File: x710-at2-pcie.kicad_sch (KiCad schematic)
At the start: 10 parts, among them U1 EZX710AT2_S_LMR5

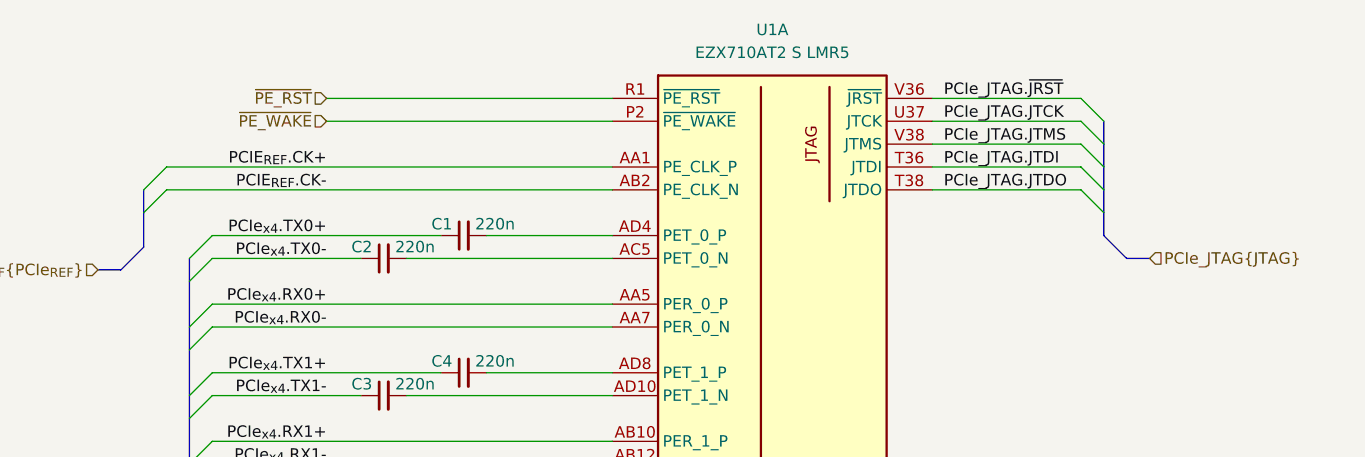
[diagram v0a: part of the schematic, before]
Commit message: [#80813] Add RJ45 connectors, add SMBus, FLASH SPI and misc
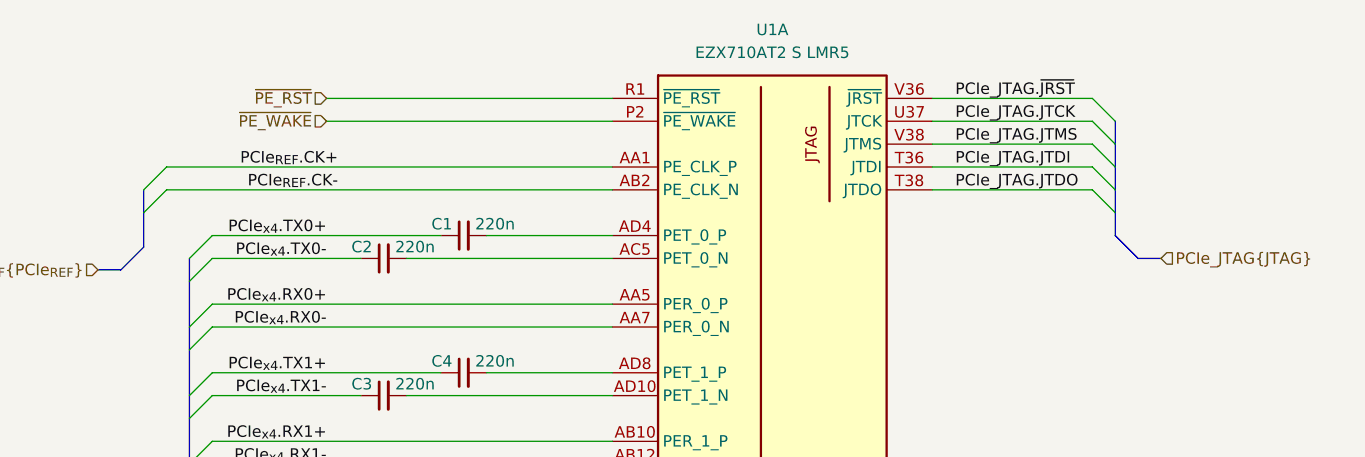
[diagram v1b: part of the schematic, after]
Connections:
- net PCIE_{REF}.CK+ renamed PCIe_{REF}.CK+
- net PCIE_{REF}.CK- renamed PCIe_{REF}.CK-
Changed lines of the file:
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@@
 		(comment 1 "www.antmicro.com")
+	)
+	(bus_alias "JTAG"
+		(members "~{JRST}" "JTCK" "JTMS" "JTDI" "JTDO")
+	)
+	(bus_alias "PCIe"
+		(members "TX7+" "TX7-" "TX6+" "TX6-" "TX5+" "TX5-" "TX4+" "TX4-" "TX3+"
+			"TX3-" "TX2+" "TX2-" "TX1+" "TX1-" "TX0+" "TX0-" "RX7+" "RX7-" "RX6+"
+			"RX6-" "RX5+" "RX5-" "RX4+" "RX4-" "RX3+" "RX3-" "RX2+" "RX2-" "RX1+"
+			"RX1-" "RX0+" "RX0-"
+		)
 	)
 	(bus_alias "PCIe_{REF}"
@@
 	)
 	(bus_entry
-		(at 248.92 102.87)
+		(at 250.19 102.87)
 		(size -2.54 -2.54)
 		(stroke
@@
 	)
 	(bus_entry
-		(at 248.92 100.33)
+		(at 250.19 100.33)
 		(size -2.54 -2.54)
 		(stroke
@@
 	)
 	(bus_entry
-		(at 248.92 95.25)
+		(at 250.19 95.25)
 		(size -2.54 -2.54)
 		(stroke
@@
 	)
 	(bus_entry
-		(at 248.92 97.79)
+		(at 250.19 97.79)
 		(size -2.54 -2.54)
 		(stroke
@@
 	)
 	(bus_entry
-		(at 248.92 105.41)
+		(at 250.19 105.41)
 		(size -2.54 -2.54)
 		(stroke
@@
 		)
 	)
-	(wire
-		(pts
-			(xy 229.87 92.71) (xy 246.38 92.71)
-		)
-		(stroke
-			(width 0)
-			(type default)
-		)
-	)
 	(bus
 		(pts
@@
 		)
 	)
-	(wire
-		(pts
-			(xy 229.87 95.25) (xy 246.38 95.25)
-		)
-		(stroke
-			(width 0)
-			(type default)
-		)
-	)
-	(bus
-		(pts
-			(xy 248.92 105.41) (xy 248.92 107.95)
+	(bus
+		(pts
+			(xy 250.19 105.41) (xy 250.19 107.95)
 		)
 		(stroke
@@
 	(wire
 		(pts
-			(xy 229.87 97.79) (xy 246.38 97.79)
-		)
-		(stroke
-			(width 0)
-			(type default)
-		)
-	)
-	(wire
-		(pts
 			(xy 149.86 133.35) (xy 194.31 133.35)
 		)
@@
 		)
 	)
-	(bus
-		(pts
-			(xy 251.46 110.49) (xy 254 110.49)
+	(wire
+		(pts
+			(xy 229.87 95.25) (xy 247.65 95.25)
+		)
+		(stroke
+			(width 0)
+			(type default)
+		)
+	)
+	(bus
+		(pts
+			(xy 252.73 110.49) (xy 255.27 110.49)
 		)
 		(stroke
@@
 		)
 	)
-	(bus
-		(pts
-			(xy 248.92 97.79) (xy 248.92 100.33)
+	(wire
+		(pts
+			(xy 229.87 92.71) (xy 247.65 92.71)
+		)
+		(stroke
+			(width 0)
+			(type default)
+		)
+	)
+	(bus
+		(pts
+			(xy 250.19 97.79) (xy 250.19 100.33)
 		)
 		(stroke
@@
 	(wire
 		(pts
+			(xy 229.87 100.33) (xy 247.65 100.33)
+		)
+		(stroke
+			(width 0)
+			(type default)
+		)
+	)
+	(wire
+		(pts
 			(xy 149.86 130.81) (xy 194.31 130.81)
 		)
@@
 	(wire
 		(pts
+			(xy 229.87 102.87) (xy 247.65 102.87)
+		)
+		(stroke
+			(width 0)
+			(type default)
+		)
+	)
+	(wire
+		(pts
 			(xy 180.34 123.19) (xy 194.31 123.19)
 		)
@@
 	(bus
 		(pts
-			(xy 251.46 110.49) (xy 248.92 107.95)
+			(xy 252.73 110.49) (xy 250.19 107.95)
 		)
 		(stroke
@@
 	(wire
 		(pts
-			(xy 229.87 102.87) (xy 246.38 102.87)
-		)
-		(stroke
-			(width 0)
-			(type default)
-		)
-	)
-	(wire
-		(pts
 			(xy 171.45 125.73) (xy 194.31 125.73)
 		)
@@
 	(bus
 		(pts
-			(xy 248.92 102.87) (xy 248.92 105.41)
+			(xy 250.19 102.87) (xy 250.19 105.41)
 		)
 		(stroke
@@
 	(wire
 		(pts
+			(xy 229.87 97.79) (xy 247.65 97.79)
+		)
+		(stroke
+			(width 0)
+			(type default)
+		)
+	)
+	(wire
+		(pts
 			(xy 149.86 115.57) (xy 194.31 115.57)
 		)
@@
 		)
 	)
-	(wire
-		(pts
-			(xy 229.87 100.33) (xy 246.38 100.33)
-		)
-		(stroke
-			(width 0)
-			(type default)
-		)
-	)
-	(bus
-		(pts
-			(xy 248.92 100.33) (xy 248.92 102.87)
-		)
-		(stroke
-			(width 0)
-			(type default)
-		)
-	)
-	(bus
-		(pts
-			(xy 248.92 95.25) (xy 248.92 97.79)
+	(bus
+		(pts
+			(xy 250.19 100.33) (xy 250.19 102.87)
+		)
+		(stroke
+			(width 0)
+			(type default)
+		)
+	)
+	(bus
+		(pts
+			(xy 250.19 95.25) (xy 250.19 97.79)
 		)
 		(stroke
@@
 	)
 	(label "PCIe_JTAG.~{JRST}"
-		(at 231.14 92.71 0)
+		(at 232.41 92.71 0)
 		(effects
 			(font
@@
 	)
 	(label "PCIe_JTAG.JTDI"
-		(at 231.14 100.33 0)
+		(at 232.41 100.33 0)
 		(effects
 			(font
@@
 	)
 	(label "PCIe_JTAG.JTMS"
-		(at 231.14 97.79 0)
+		(at 232.41 97.79 0)
 		(effects
 			(font
@@
 		)
 	)
+	(label "PCIe_{REF}.CK-"
+		(at 163.83 102.87 180)
+		(effects
+			(font
+				(size 1.27 1.27)
+			)
+			(justify right bottom)
+		)
+	)
 	(label "PCIe_{x4}.TX0+"
 		(at 162.56 107.95 180)
@@
 		)
 	)
-	(label "PCIE_{REF}.CK-"
-		(at 162.56 102.87 180)
-		(effects
-			(font
-				(size 1.27 1.27)
-			)
-			(justify right bottom)
-		)
-	)
-	(label "PCIE_{REF}.CK+"
-		(at 162.56 100.33 180)
-		(effects
-			(font
-				(size 1.27 1.27)
-			)
-			(justify right bottom)
-		)
-	)
 	(label "PCIe_{x4}.RX1+"
 		(at 162.56 130.81 180)
@@
 	)
 	(label "PCIe_JTAG.JTCK"
-		(at 231.14 95.25 0)
+		(at 232.41 95.25 0)
 		(effects
 			(font
@@
 			)
 			(justify left bottom)
+		)
+	)
+	(label "PCIe_{REF}.CK+"
+		(at 163.83 100.33 180)
+		(effects
+			(font
+				(size 1.27 1.27)
+			)
+			(justify right bottom)
 		)
 	)
@@
 	)
 	(label "PCIe_JTAG.JTDO"
-		(at 231.14 102.87 0)
+		(at 232.41 102.87 0)
 		(effects
 			(font
@@
 	(hierarchical_label "PCIe_JTAG{JTAG}"
 		(shape input)
-		(at 254 110.49 0)
-		(effects
-			(font
+		(at 255.27 110.49 0)
+		(effects
+			(font

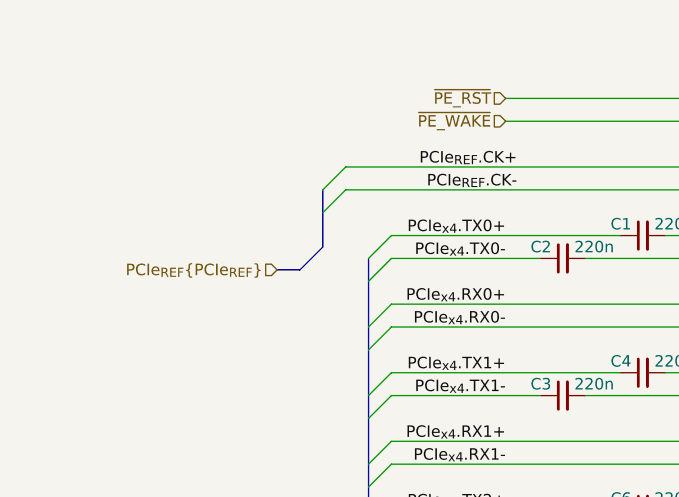
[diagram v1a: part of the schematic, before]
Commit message: [#80813] Add misc, improve schematic readability
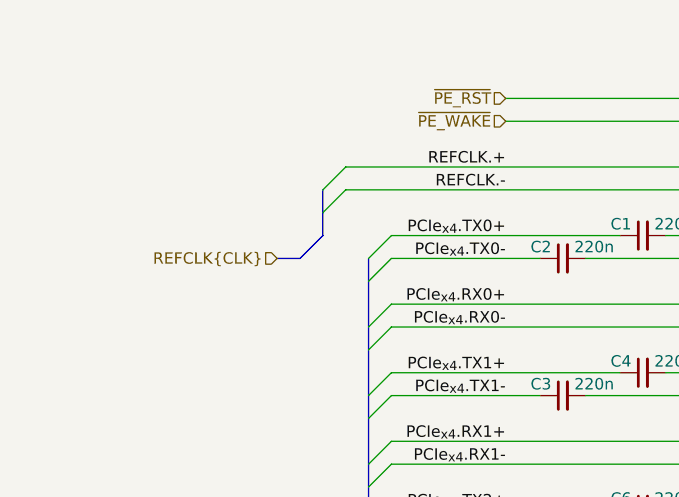
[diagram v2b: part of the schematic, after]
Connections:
- net PCIe_{REF}.CK+ renamed REFCLK.+
- net PCIe_{REF}.CK- renamed REFCLK.-
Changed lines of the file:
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@@
 		(comment 1 "www.antmicro.com")
+	)
+	(bus_alias "CLK"
+		(members "+" "-")
 	)
 	(bus_alias "JTAG"
@@
 		)
 	)
-	(bus_alias "PCIe_{REF}"
-		(members "CK+" "CK-")
-	)
 	(no_connect
 		(at 194.31 171.45)
@@
 	(bus
 		(pts
-			(xy 142.24 105.41) (xy 142.24 109.22)
+			(xy 142.24 105.41) (xy 142.24 107.95)
 		)
 		(stroke
@@
 	(bus
 		(pts
-			(xy 137.16 111.76) (xy 139.7 111.76)
+			(xy 137.16 110.49) (xy 139.7 110.49)
 		)
 		(stroke
@@
 	(bus
 		(pts
-			(xy 139.7 111.76) (xy 142.24 109.22)
+			(xy 139.7 110.49) (xy 142.24 107.95)
 		)
 		(stroke
@@
 		)
 	)
-	(label "PCIe_{REF}.CK-"
-		(at 163.83 102.87 180)
+	(label "REFCLK.-"
+		(at 162.56 102.87 180)
 		(effects
 			(font
@@
 		)
 	)
-	(label "PCIe_{REF}.CK+"
-		(at 163.83 100.33 180)
+	(label "REFCLK.+"
+		(at 162.56 100.33 180)
 		(effects
 			(font
@@
 		)
 	)
-	(hierarchical_label "PCIe_{REF}{PCIe_{REF}}"
+	(hierarchical_label "REFCLK{CLK}"
 		(shape input)
-		(at 137.16 111.76 180)
-		(effects
-			(font
+		(at 137.16 110.49 180)
+		(effects
+			(font

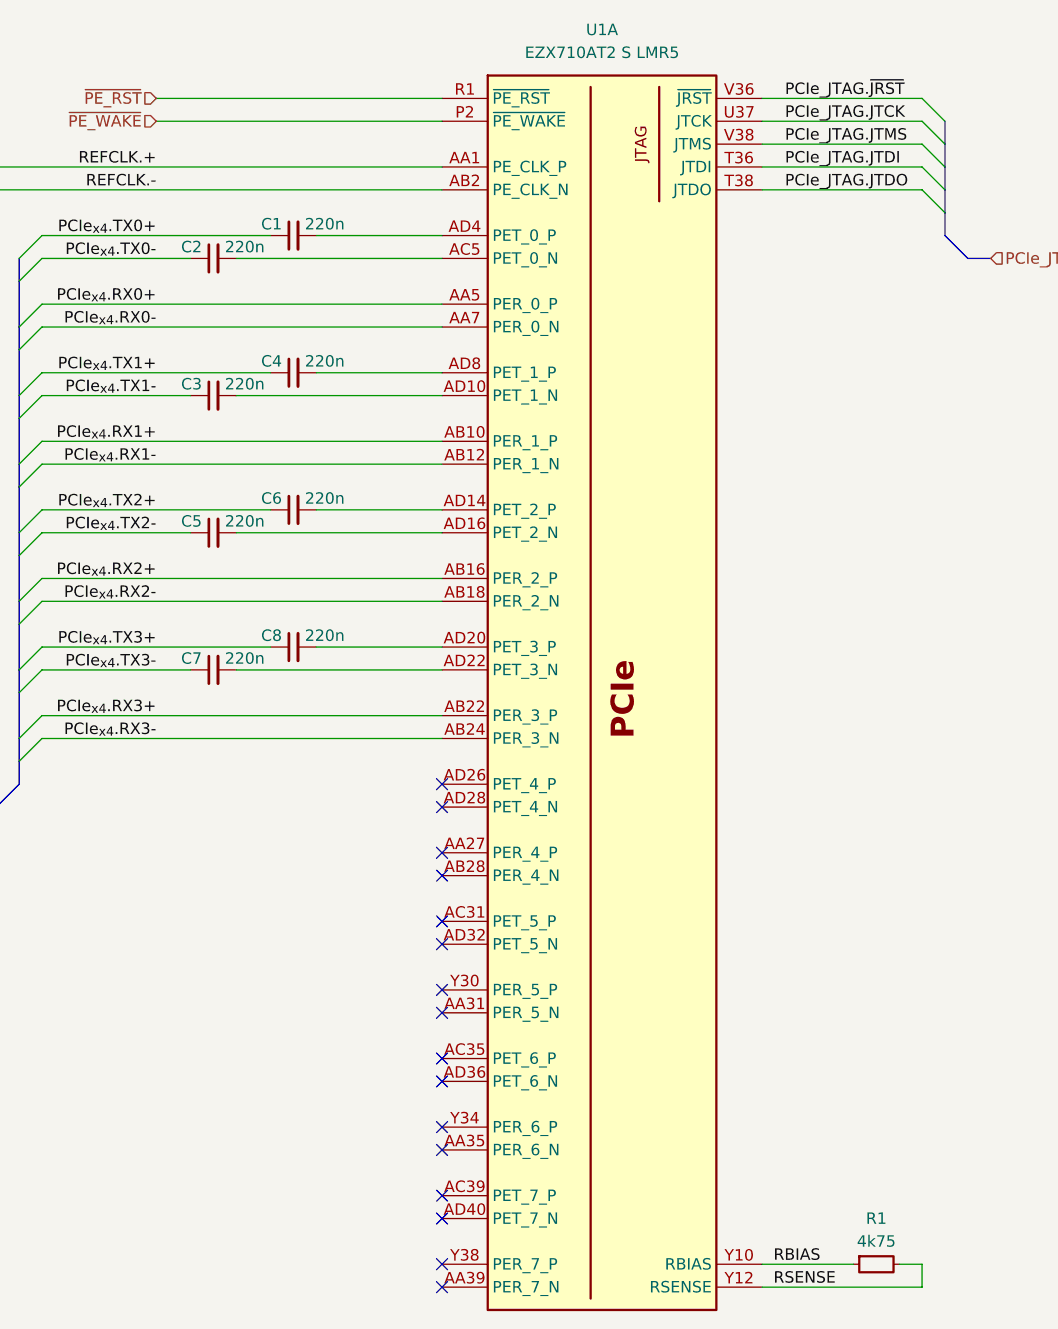
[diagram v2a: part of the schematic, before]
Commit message: [#80813] Change RJ45 connectors, reannotate schematics
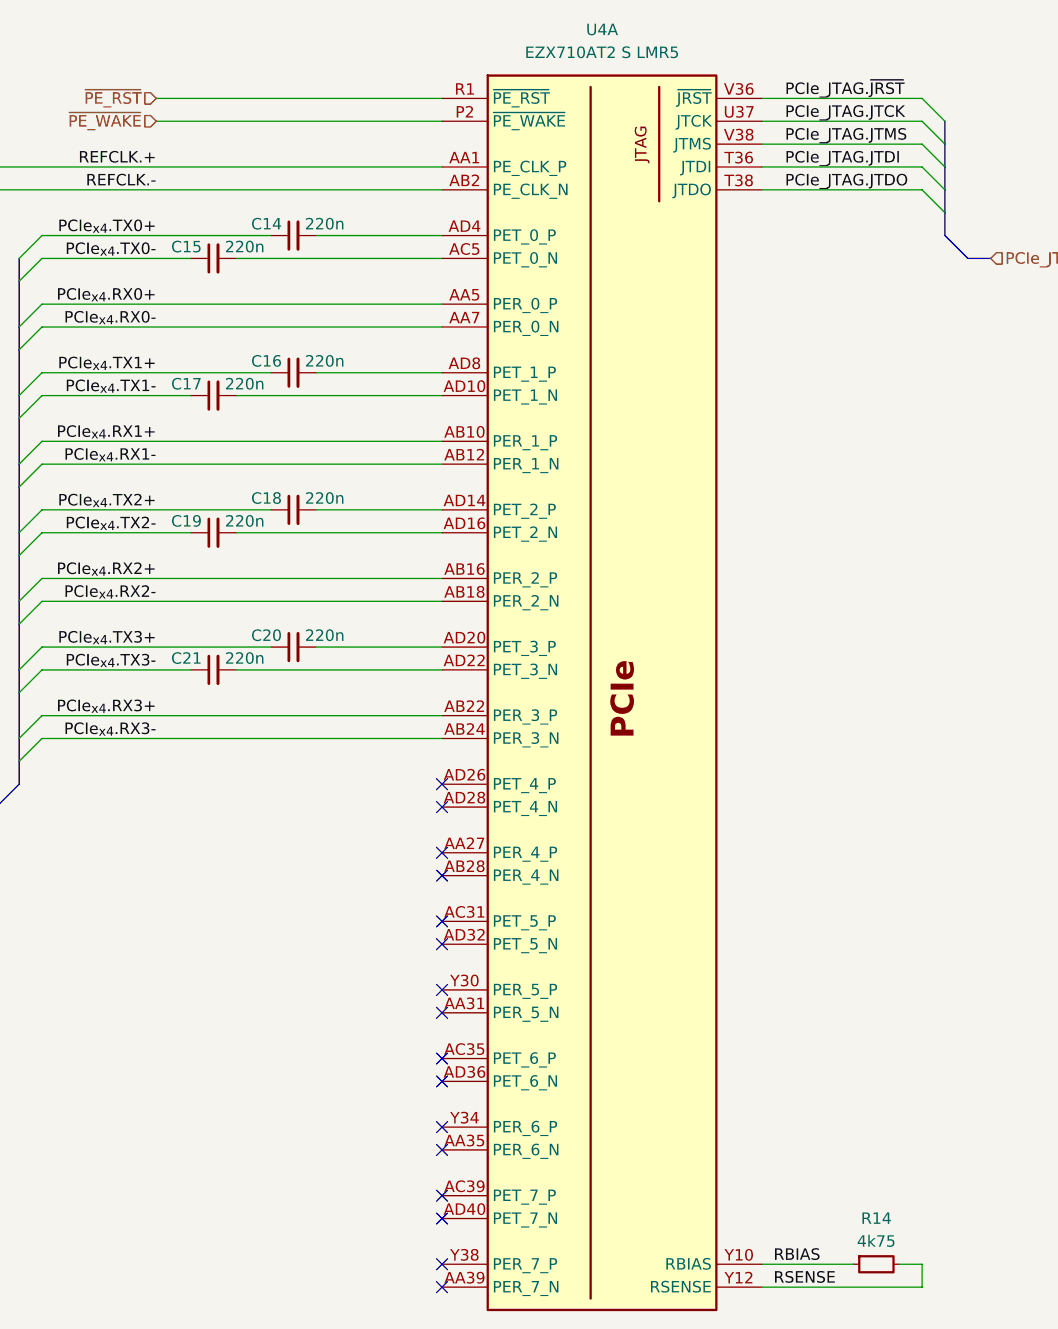
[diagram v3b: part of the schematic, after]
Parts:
- renumbered C1 to C14, C2 to C15, C4 to C16, C3 to C17, C6 to C18, C5 to C19, C8 to C20, C7 to C21, R1 to R14, U1 to U4
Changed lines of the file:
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@@
 		(on_board yes)
 		(dnp no)
-		(property "Reference" "C8"
+		(property "Reference" "C20"
 			(at 176.53 152.4 0)
 			(effects
@@
 			(project "10-gbe-expansion"
 				(path "/04bda987-e5eb-48b4-9e90-d8211dc11b39/2e3e9f9b-8e60-4e62-87df-aa866913a2fb"
-					(reference "C8")
+					(reference "C20")
 					(unit 1)
 				)
@@
 		(on_board yes)
 		(dnp no)
-		(property "Reference" "R1"
+		(property "Reference" "R14"
 			(at 242.57 217.17 0)
 			(effects
@@
 			(project "10-gbe-expansion"
 				(path "/04bda987-e5eb-48b4-9e90-d8211dc11b39/2e3e9f9b-8e60-4e62-87df-aa866913a2fb"
-					(reference "R1")
+					(reference "R14")
 					(unit 1)
 				)
@@
 		(on_board yes)
 		(dnp no)
-		(property "Reference" "C6"
+		(property "Reference" "C18"
 			(at 176.53 137.16 0)
 			(effects
@@
 			(project "10-gbe-expansion"
 				(path "/04bda987-e5eb-48b4-9e90-d8211dc11b39/2e3e9f9b-8e60-4e62-87df-aa866913a2fb"
-					(reference "C6")
+					(reference "C18")
 					(unit 1)
 				)
@@
 		(on_board yes)
 		(dnp no)
-		(property "Reference" "C5"
+		(property "Reference" "C19"
 			(at 167.64 139.7 0)
 			(effects
@@
 			(project "10-gbe-expansion"
 				(path "/04bda987-e5eb-48b4-9e90-d8211dc11b39/2e3e9f9b-8e60-4e62-87df-aa866913a2fb"
-					(reference "C5")
+					(reference "C19")
 					(unit 1)
 				)
@@
 		(on_board yes)
 		(dnp no)
-		(property "Reference" "C2"
+		(property "Reference" "C15"
 			(at 167.64 109.22 0)
 			(effects
@@
 			(project "10-gbe-expansion"
 				(path "/04bda987-e5eb-48b4-9e90-d8211dc11b39/2e3e9f9b-8e60-4e62-87df-aa866913a2fb"
-					(reference "C2")
+					(reference "C15")
 					(unit 1)
 				)
@@
 		(on_board yes)
 		(dnp no)
-		(property "Reference" "C3"
+		(property "Reference" "C17"
 			(at 167.64 124.46 0)
 			(effects
@@
 			(project "10-gbe-expansion"
 				(path "/04bda987-e5eb-48b4-9e90-d8211dc11b39/2e3e9f9b-8e60-4e62-87df-aa866913a2fb"
-					(reference "C3")
+					(reference "C17")
 					(unit 1)
 				)
@@
 		(on_board yes)
 		(dnp no)
-		(property "Reference" "C1"
+		(property "Reference" "C14"
 			(at 176.53 106.68 0)
 			(effects
@@
 			(project "10-gbe-expansion"
 				(path "/04bda987-e5eb-48b4-9e90-d8211dc11b39/2e3e9f9b-8e60-4e62-87df-aa866913a2fb"
-					(reference "C1")
+					(reference "C14")
 					(unit 1)
 				)
@@
 		(on_board yes)
 		(dnp no)
-		(property "Reference" "C4"
+		(property "Reference" "C16"
 			(at 176.53 121.92 0)
 			(effects
@@
 			(project "10-gbe-expansion"
 				(path "/04bda987-e5eb-48b4-9e90-d8211dc11b39/2e3e9f9b-8e60-4e62-87df-aa866913a2fb"
-					(reference "C4")
+					(reference "C16")
 					(unit 1)
 				)
@@
 		(on_board yes)
 		(dnp no)
-		(property "Reference" "C7"
+		(property "Reference" "C21"
 			(at 167.64 154.94 0)
 			(effects
@@
 			(project "10-gbe-expansion"
 				(path "/04bda987-e5eb-48b4-9e90-d8211dc11b39/2e3e9f9b-8e60-4e62-87df-aa866913a2fb"
-					(reference "C7")
+					(reference "C21")
 					(unit 1)
 				)
@@
 		(dnp no)
 		(fields_autoplaced yes)
-		(property "Reference" "U1"
+		(property "Reference" "U4"
 			(at 212.09 85.09 0)
 			(effects
@@
 			(project "10-gbe-expansion"
 				(path "/04bda987-e5eb-48b4-9e90-d8211dc11b39/2e3e9f9b-8e60-4e62-87df-aa866913a2fb"
-					(reference "U1")
+					(reference "U4")
 					(unit 1)
 				)
